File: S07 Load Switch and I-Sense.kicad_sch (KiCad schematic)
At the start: 66 parts, among them Q20 BSS138, Q21 BSS138, Q22 BSS138, Q24 BSS138, U10 TLV9002IDSG, U6 TPS22811, U7 TPS22811, U8 TLV9002IDSG, U9 TPS22811

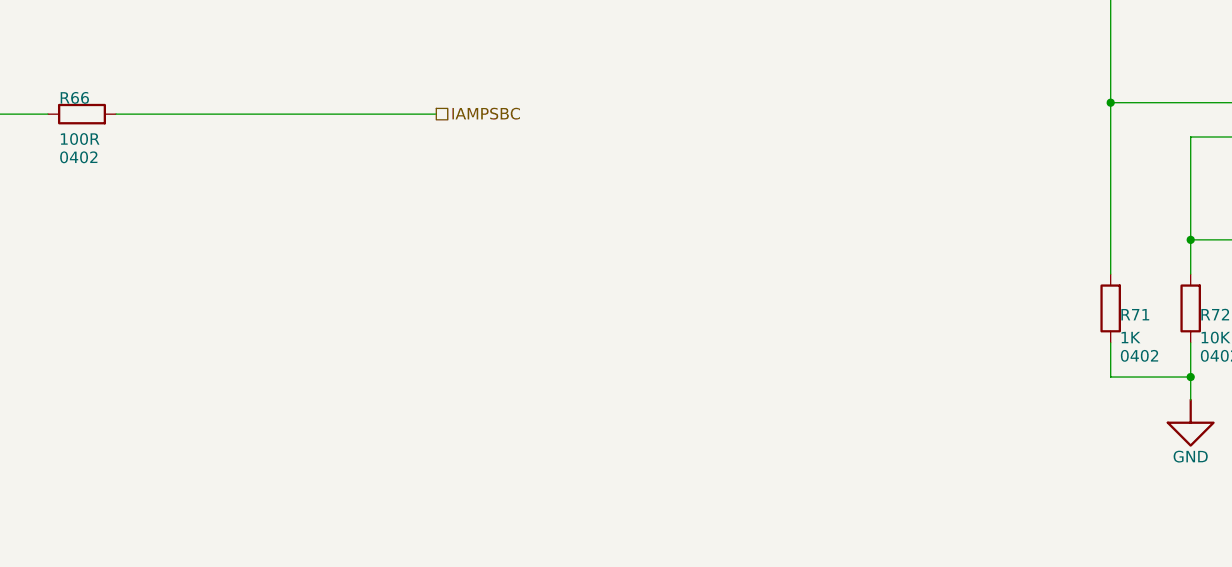
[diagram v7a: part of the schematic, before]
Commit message: R16 to 3 mOhm; note the DAQ/EXT current limits; keep Q18
- R16 0.005R -> 0.003R (Bourns CRE2512-FZ-R003E-3): the LTC1960 breaker
  moves from 18-23 A to 30-38 A. Peak 12 V load is about 7.5 A SBC (90 W)
  + 2.5 A J3 + DAQ, and QE29 packs at ~21 A would sit inside the old trip
  window. S03 note updated.
- S07 note: R53/R71 (1K, 6.6 A limit, up to 7.1 A) exceed J6/J5's 6.5 A
  single contact; raise them to 1.2K or more once the DAQ and EXT loads
  are known. Left at 1K for now: DAQ runs a stand-in, EXT is unused.
- README rows for R16, R53/R71 and Q18 (CSD17304Q3 kept: it works and 15
  units are in field test).

Co-Authored-By: Claude Opus 5.5 <noreply@anthropic.com>
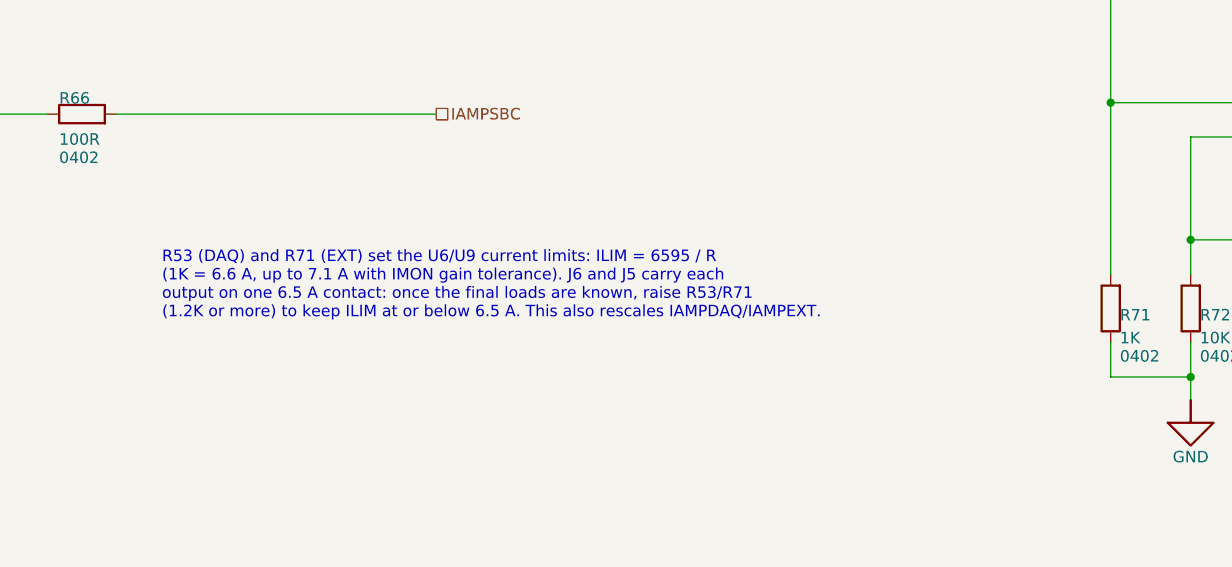
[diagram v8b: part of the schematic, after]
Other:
- note added: "R53 (DAQ) and R71 (EXT) set the U6/U9 current limits: ILIM = 6595 / R (1K = 6.6 A, up to 7.1 A with IMON gain tolerance). J6 and J5 carry each output on one 6.5 A contact: once the final loads are known, raise R53/R71 (1.2K or more) to keep ILIM at or below 6.5 A. This also rescales IAMPDAQ/IAMPEXT."
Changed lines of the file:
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@@
 	(generator_version "10.0")
 	(paper "A3")
+	(text "R53 (DAQ) and R71 (EXT) set the U6/U9 current limits: ILIM = 6595 / R\n(1K = 6.6 A, up to 7.1 A with IMON gain tolerance). J6 and J5 carry each\noutput on one 6.5 A contact: once the final loads are known, raise R53/R71\n(1.2K or more) to keep ILIM at or below 6.5 A. This also rescales IAMPDAQ/IAMPEXT."
+		(exclude_from_sim no)
+		(at 157.48 135.89 0)
+		(effects
+			(font
+				(size 1.27 1.27)
+			)
+			(justify left top)
+		)
+	)
 	(text "DAQ (U6) is deliberately different from SBC and EXT; keep it.\nU6 has an 11 V undervoltage lockout: R108/R49 turn it on at\n11.2 V (10.8-11.7 V) and off at 10.2 V (9.8-10.7 V). That\ndivider must hold EN/UVLO, so the enable goes through Q24:\nnENDAQ is active LOW. High or floating (POR, expander in reset\nor unpowered) turns Q24 on and holds U6 in shutdown; low hands\nEN/UVLO to the divider. R109/R110 bias the gate from +12V, not\n+3V3MCU, so DAQ stays off when the MCU board is unpowered."
 		(exclude_from_sim no)
